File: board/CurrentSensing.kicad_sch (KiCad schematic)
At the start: 11 parts, among them IC1 ACS37010LLZATR-030B3, IC2 ACS37010LLZATR-030B3, IC3 ACS37010LLZATR-030B3, IC4 ACS37010LLZATR-030B3, IC6 ACS37010LLZATR-030B3

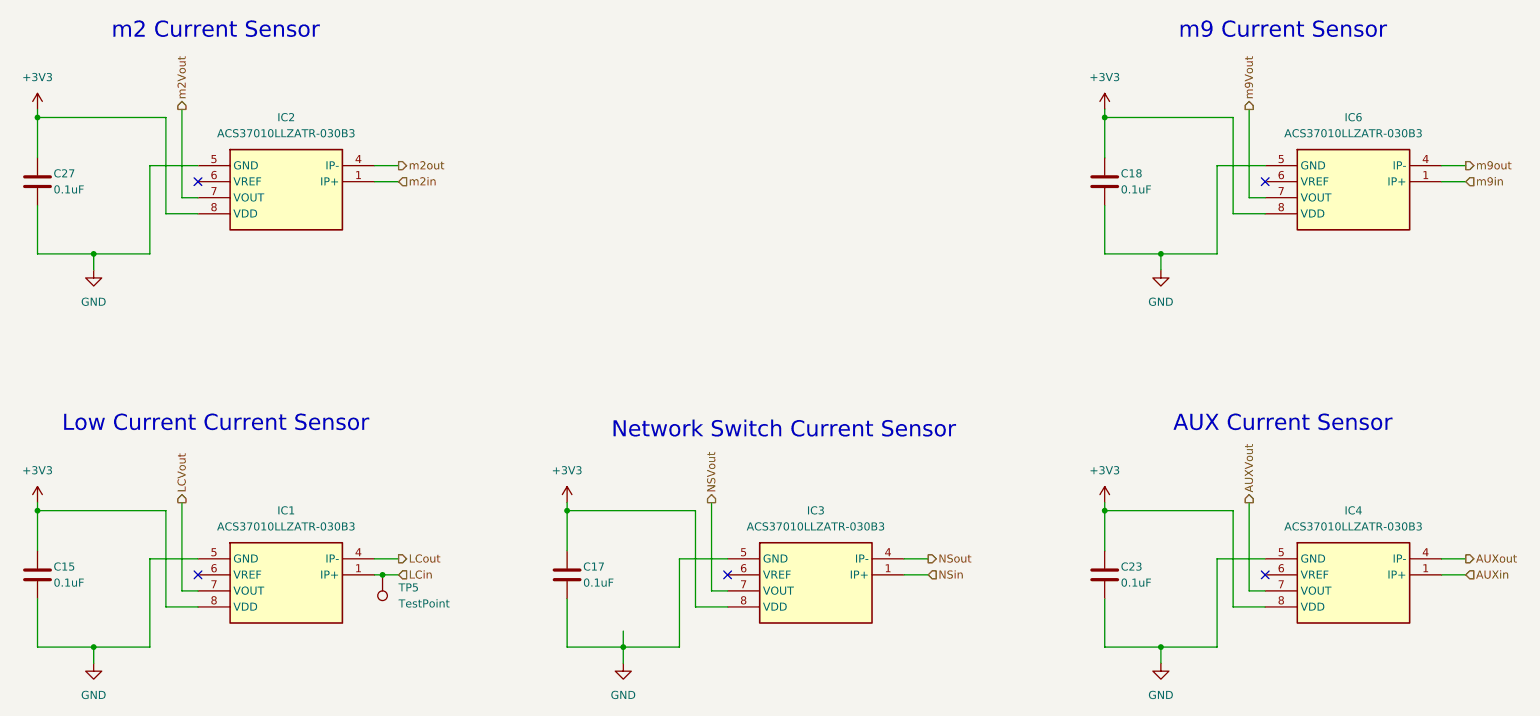
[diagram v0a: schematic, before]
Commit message: Center schematics and layout for prettiness
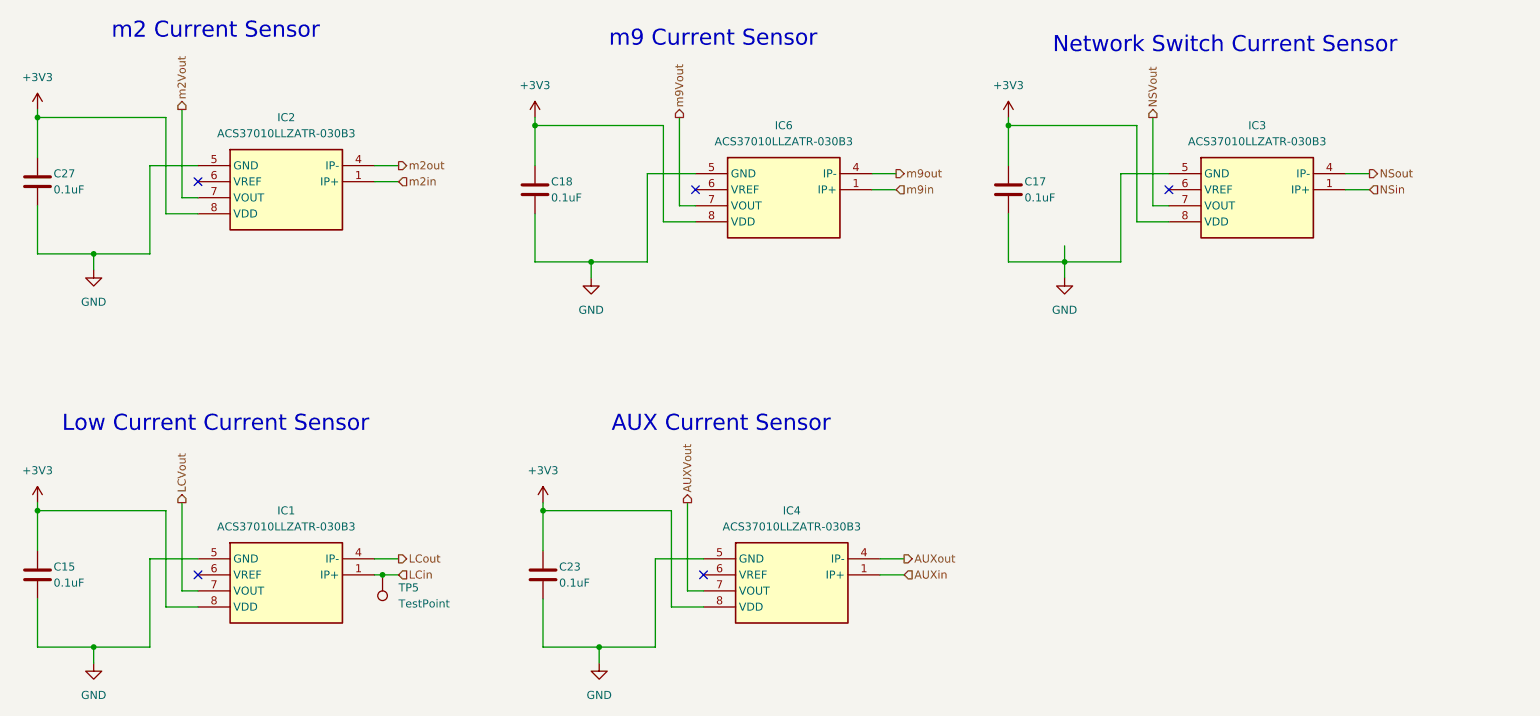
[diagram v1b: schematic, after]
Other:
- moved on the sheet: C17, C18, C23, IC3, IC4, IC6

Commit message: add label for battery sensing molex connector
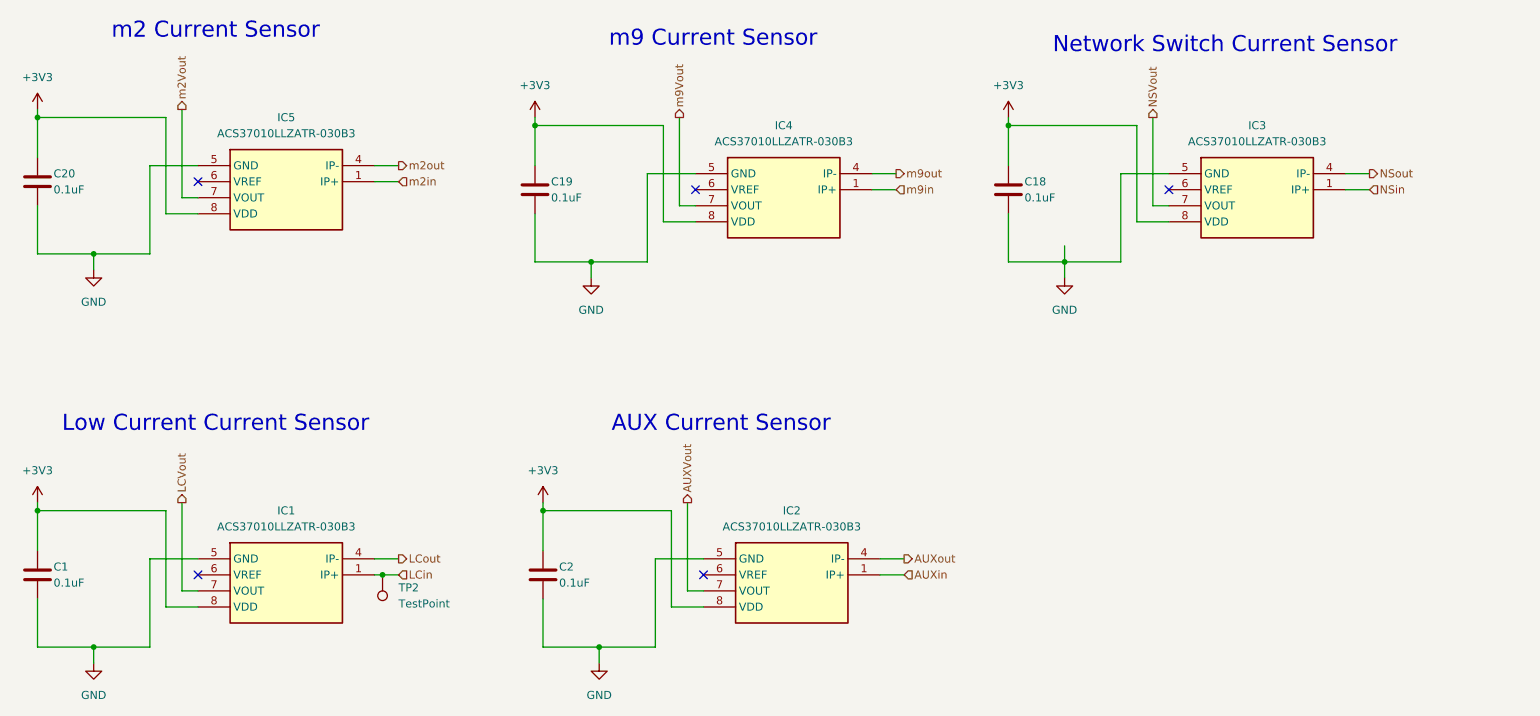
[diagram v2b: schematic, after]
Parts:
- renumbered C15 to C1, C17 to C18, C18 to C19, C23 to C2, C27 to C20, IC4 to IC2, IC6 to IC4, IC2 to IC5, TP5 to TP2
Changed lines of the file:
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@@
 		(on_board yes)
 		(dnp no)
-		(property "Reference" "C15"
+		(property "Reference" "C1"
 			(at 38.1 118.11 0)
 			(effects
@@
 			(project "PowerManagementBoard"
 				(path "/7eaa639d-7062-45e7-be05-1c2855431307/553f5510-83a4-4a32-8cf5-5f8ae000bb74"
-					(reference "C15")
+					(reference "C1")
 					(unit 1)
 				)
@@
 		(on_board yes)
 		(dnp no)
-		(property "Reference" "C23"
+		(property "Reference" "C2"
 			(at 118.11 118.11 0)
 			(effects
@@
 			(project "PowerManagementBoard"
 				(path "/7eaa639d-7062-45e7-be05-1c2855431307/553f5510-83a4-4a32-8cf5-5f8ae000bb74"
-					(reference "C23")
+					(reference "C2")
 					(unit 1)
 				)
@@
 		(dnp no)
 		(fields_autoplaced yes)
-		(property "Reference" "IC4"
+		(property "Reference" "IC2"
 			(at 154.94 109.22 0)
 			(effects
@@
 			(project "PowerManagementBoard"
 				(path "/7eaa639d-7062-45e7-be05-1c2855431307/553f5510-83a4-4a32-8cf5-5f8ae000bb74"
-					(reference "IC4")
+					(reference "IC2")
 					(unit 1)
 				)
@@
 		(on_board yes)
 		(dnp no)
-		(property "Reference" "C27"
+		(property "Reference" "C20"
 			(at 38.1 55.88 0)
 			(effects
@@
 			(project "PowerManagementBoard"
 				(path "/7eaa639d-7062-45e7-be05-1c2855431307/553f5510-83a4-4a32-8cf5-5f8ae000bb74"
-					(reference "C27")
+					(reference "C20")
 					(unit 1)
 				)
@@
 		(on_board yes)
 		(dnp no)
-		(property "Reference" "C17"
+		(property "Reference" "C18"
 			(at 191.77 57.15 0)
 			(effects
@@
 			(project "PowerManagementBoard"
 				(path "/7eaa639d-7062-45e7-be05-1c2855431307/553f5510-83a4-4a32-8cf5-5f8ae000bb74"
-					(reference "C17")
+					(reference "C18")
 					(unit 1)
 				)
@@
 		(on_board yes)
 		(dnp no)
-		(property "Reference" "C18"
+		(property "Reference" "C19"
 			(at 116.84 57.15 0)
 			(effects
@@
 			(project "PowerManagementBoard"
 				(path "/7eaa639d-7062-45e7-be05-1c2855431307/553f5510-83a4-4a32-8cf5-5f8ae000bb74"
-					(reference "C18")
+					(reference "C19")
 					(unit 1)
 				)
@@
 		(dnp no)
 		(fields_autoplaced yes)
-		(property "Reference" "IC6"
+		(property "Reference" "IC4"
 			(at 153.67 48.26 0)
 			(effects
@@
 			(project "PowerManagementBoard"
 				(path "/7eaa639d-7062-45e7-be05-1c2855431307/553f5510-83a4-4a32-8cf5-5f8ae000bb74"
-					(reference "IC6")
+					(reference "IC4")
 					(unit 1)
 				)
@@
 		(dnp no)
 		(fields_autoplaced yes)
-		(property "Reference" "TP5"
+		(property "Reference" "TP2"
 			(at 92.71 121.4119 0)
 			(effects
@@
 			(project "PowerManagementBoard"
 				(path "/7eaa639d-7062-45e7-be05-1c2855431307/553f5510-83a4-4a32-8cf5-5f8ae000bb74"
-					(reference "TP5")
+					(reference "TP2")
 					(unit 1)
 				)
@@
 		(dnp no)
 		(fields_autoplaced yes)
-		(property "Reference" "IC2"
+		(property "Reference" "IC5"
 			(at 74.93 46.99 0)
 			(effects
@@
 			(project "PowerManagementBoard"
 				(path "/7eaa639d-7062-45e7-be05-1c2855431307/553f5510-83a4-4a32-8cf5-5f8ae000bb74"
-					(reference "IC2")
-					(unit 1)
-				)
+					(reference "IC5")
+					(unit 1)
+				)

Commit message: Testing points started
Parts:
- added TP8, TP9: TestPoint, TestPoint:TestPoint_Pad_D1.0mm, symbol Connector:TestPoint
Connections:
- net AUXin: now also TP9.1
- net NSout: now also TP8.1
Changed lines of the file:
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@@
+	)
+	(junction
+		(at 243.84 55.88)
+		(diameter 0)
+		(color 0 0 0 0)
 	)
 	(junction
@@
 	)
 	(junction
+		(at 170.18 119.38)
+		(diameter 0)
+		(color 0 0 0 0)
+	)
+	(junction
 		(at 123.19 69.85)
 		(diameter 0)
@@
 	(wire
 		(pts
-			(xy 242.57 55.88) (xy 246.38 55.88)
+			(xy 242.57 55.88) (xy 243.84 55.88)
 		)
 		(stroke
@@
 	(wire
 		(pts
+			(xy 243.84 55.88) (xy 246.38 55.88)
+		)
+		(stroke
+			(width 0)
+			(type default)
+		)
+	)
+	(wire
+		(pts
+			(xy 60.96 124.46) (xy 55.88 124.46)
+		)
+		(stroke
+			(width 0)
+			(type default)
+		)
+	)
+	(wire
+		(pts
+			(xy 214.63 63.5) (xy 209.55 63.5)
+		)
+		(stroke
+			(width 0)
+			(type default)
+		)
+	)
+	(wire
+		(pts
+			(xy 167.64 58.42) (xy 171.45 58.42)
+		)
+		(stroke
+			(width 0)
+			(type default)
+		)
+	)
+	(wire
+		(pts
+			(xy 35.56 107.95) (xy 35.56 109.22)
+		)
+		(stroke
+			(width 0)
+			(type default)
+		)
+	)
+	(wire
+		(pts
+			(xy 198.12 69.85) (xy 198.12 72.39)
+		)
+		(stroke
+			(width 0)
+			(type default)
+		)
+	)
+	(wire
+		(pts
+			(xy 198.12 69.85) (xy 207.01 69.85)
+		)
+		(stroke
+			(width 0)
+			(type default)
+		)
+	)
+	(wire
+		(pts
+			(xy 212.09 60.96) (xy 214.63 60.96)
+		)
+		(stroke
+			(width 0)
+			(type default)
+		)
+	)
+	(wire
+		(pts
+			(xy 114.3 46.99) (xy 114.3 48.26)
+		)
+		(stroke
+			(width 0)
+			(type default)
+		)
+	)
+	(wire
+		(pts
+			(xy 58.42 59.69) (xy 60.96 59.69)
+		)
+		(stroke
+			(width 0)
+			(type default)
+		)
+	)
+	(wire
+		(pts
+			(xy 207.01 69.85) (xy 207.01 55.88)
+		)
+		(stroke
+			(width 0)
+			(type default)
+		)
+	)
+	(wire
+		(pts
+			(xy 90.17 119.38) (xy 92.71 119.38)
+		)
+		(stroke
+			(width 0)
+			(type default)
+		)
+	)
+	(wire
+		(pts
+			(xy 35.56 46.99) (xy 35.56 53.34)
+		)
+		(stroke
+			(width 0)
+			(type default)
+		)
+	)
+	(wire
+		(pts
+			(xy 133.35 130.81) (xy 133.35 116.84)
+		)
+		(stroke
+			(width 0)
+			(type default)
+		)
+	)
+	(wire
+		(pts
+			(xy 35.56 68.58) (xy 44.45 68.58)
+		)
+		(stroke
+			(width 0)
+			(type default)
+		)
+	)
+	(wire
+		(pts
+			(xy 123.19 69.85) (xy 123.19 72.39)
+		)
+		(stroke
+			(width 0)
+			(type default)
+		)
+	)
+	(wire
+		(pts
 			(xy 167.64 55.88) (xy 171.45 55.88)
 		)
@@
 	(wire
 		(pts
-			(xy 60.96 124.46) (xy 55.88 124.46)
-		)
-		(stroke
-			(width 0)
-			(type default)
-		)
-	)
-	(wire
-		(pts
-			(xy 214.63 63.5) (xy 209.55 63.5)
-		)
-		(stroke
-			(width 0)
-			(type default)
-		)
-	)
-	(wire
-		(pts
-			(xy 167.64 58.42) (xy 171.45 58.42)
-		)
-		(stroke
-			(width 0)
-			(type default)
-		)
-	)
-	(wire
-		(pts
-			(xy 35.56 107.95) (xy 35.56 109.22)
-		)
-		(stroke
-			(width 0)
-			(type default)
-		)
-	)
-	(wire
-		(pts
-			(xy 198.12 69.85) (xy 198.12 72.39)
-		)
-		(stroke
-			(width 0)
-			(type default)
-		)
-	)
-	(wire
-		(pts
-			(xy 198.12 69.85) (xy 207.01 69.85)
-		)
-		(stroke
-			(width 0)
-			(type default)
-		)
-	)
-	(wire
-		(pts
-			(xy 212.09 60.96) (xy 214.63 60.96)
-		)
-		(stroke
-			(width 0)
-			(type default)
-		)
-	)
-	(wire
-		(pts
-			(xy 114.3 46.99) (xy 114.3 48.26)
-		)
-		(stroke
-			(width 0)
-			(type default)
-		)
-	)
-	(wire
-		(pts
-			(xy 58.42 59.69) (xy 60.96 59.69)
-		)
-		(stroke
-			(width 0)
-			(type default)
-		)
-	)
-	(wire
-		(pts
-			(xy 207.01 69.85) (xy 207.01 55.88)
-		)
-		(stroke
-			(width 0)
-			(type default)
-		)
-	)
-	(wire
-		(pts
-			(xy 90.17 119.38) (xy 92.71 119.38)
-		)
-		(stroke
-			(width 0)
-			(type default)
-		)
-	)
-	(wire
-		(pts
-			(xy 35.56 46.99) (xy 35.56 53.34)
-		)
-		(stroke
-			(width 0)
-			(type default)
-		)
-	)
-	(wire
-		(pts
-			(xy 133.35 130.81) (xy 133.35 116.84)
-		)
-		(stroke
-			(width 0)
-			(type default)
-		)
-	)
-	(wire
-		(pts
-			(xy 35.56 68.58) (xy 44.45 68.58)
-		)
-		(stroke
-			(width 0)
-			(type default)
-		)
-	)
-	(wire
-		(pts
-			(xy 123.19 69.85) (xy 123.19 72.39)
-		)
-		(stroke
-			(width 0)
-			(type default)
-		)
-	)
-	(wire
-		(pts
 			(xy 198.12 67.31) (xy 198.12 69.85)
 		)
@@
 	(wire
 		(pts
+			(xy 170.18 119.38) (xy 172.72 119.38)
+		)
+		(stroke
+			(width 0)
+			(type default)
+		)
+	)
+	(wire
+		(pts
 			(xy 88.9 119.38) (xy 90.17 119.38)
 		)
@@
 	(wire
 		(pts
-			(xy 168.91 119.38) (xy 172.72 119.38)
+			(xy 168.91 119.38) (xy 170.18 119.38)
 		)
 		(stroke
@@
 	)
 	(symbol
+		(lib_id "Connector:TestPoint")
+		(at 243.84 55.88 0)
+		(unit 1)
+		(exclude_from_sim no)
+		(in_bom yes)
+		(on_board yes)
+		(dnp no)
+		(fields_autoplaced yes)
+		(property "Reference" "TP8"
+			(at 246.38 51.3079 0)
+			(effects
+				(font
+					(size 1.27 1.27)
+				)
+				(justify left)
+			)
+		)
+		(property "Value" "TestPoint"
+			(at 246.38 53.8479 0)
+			(effects
+				(font
+					(size 1.27 1.27)
+				)
+				(justify left)
+			)
+		)
+		(property "Footprint" "TestPoint:TestPoint_Pad_D1.0mm"
+			(at 248.92 55.88 0)
+			(effects
+				(font
+					(size 1.27 1.27)
+				)
+				(hide yes)
+			)
+		)
+		(property "Datasheet" "~"
+			(at 248.92 55.88 0)
+			(effects
+				(font
+					(size 1.27 1.27)
+				)
+				(hide yes)
+			)
+		)
+		(property "Description" "test point"
+			(at 243.84 55.88 0)
+			(effects
+				(font
+					(size 1.27 1.27)
+				)
+				(hide yes)
+			)
+		)
+		(pin "1"
+		)
+		(instances
+			(project "PowerManagementBoard"
+				(path "/7eaa639d-7062-45e7-be05-1c2855431307/553f5510-83a4-4a32-8cf5-5f8ae000bb74"
+					(reference "TP8")
+					(unit 1)
+				)
+			)
+		)
+	)
+	(symbol
 		(lib_id "power:+3V3")
 		(at 189.23 46.99 0)
@@
 					(unit 1)
 				)
+			)
+		)
+	)
+	(symbol
+		(lib_id "Connector:TestPoint")
+		(at 170.18 119.38 180)
+		(unit 1)
+		(exclude_from_sim no)
+		(in_bom yes)
+		(on_board yes)
+		(dnp no)
+		(fields_autoplaced yes)
+		(property "Reference" "TP9"
+			(at 172.72 121.4119 0)
+			(effects
+				(font
+					(size 1.27 1.27)
+				)
+				(justify right)
+			)
+		)
+		(property "Value" "TestPoint"
+			(at 172.72 123.9519 0)
+			(effects
+				(font
+					(size 1.27 1.27)
+				)
+				(justify right)
+			)
+		)
+		(property "Footprint" "TestPoint:TestPoint_Pad_D1.0mm"
+			(at 165.1 119.38 0)
+			(effects
+				(font
+					(size 1.27 1.27)
+				)
+				(hide yes)
+			)
+		)
+		(property "Datasheet" "~"
+			(at 165.1 119.38 0)
+			(effects
+				(font
+					(size 1.27 1.27)
+				)
+				(hide yes)
+			)
+		)
+		(property "Description" "test point"
+			(at 170.18 119.38 0)
+			(effects
+				(font
+					(size 1.27 1.27)
+				)
+				(hide yes)
+			)
+		)
+		(pin "1"
+		)
+		(instances
+			(project "PowerManagementBoard"
+				(path "/7eaa639d-7062-45e7-be05-1c2855431307/553f5510-83a4-4a32-8cf5-5f8ae000bb74"
+					(reference "TP9")
+					(unit 1)
+				)
